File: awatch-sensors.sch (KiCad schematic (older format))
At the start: 35 parts, among them U501 BMM150, U502 APDS-9306-065, U503 BMI160, U504 BMP388

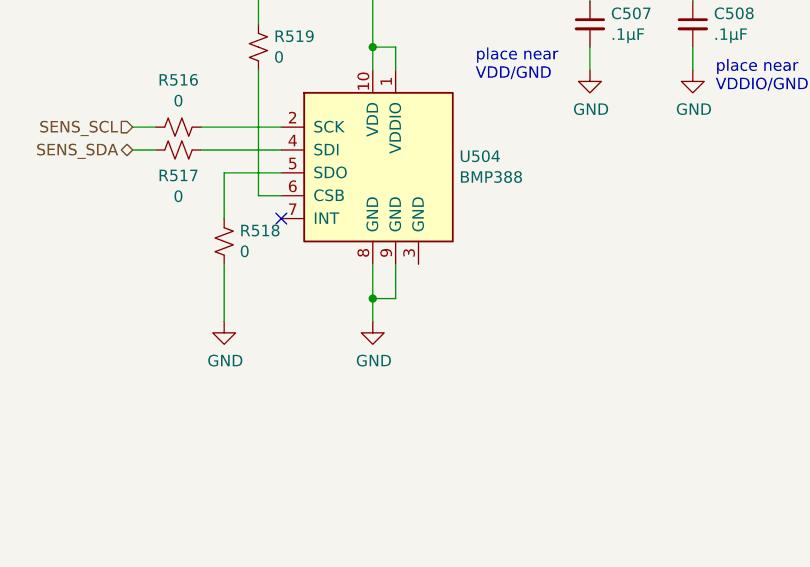
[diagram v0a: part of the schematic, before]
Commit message: Place and route pressure sensor.
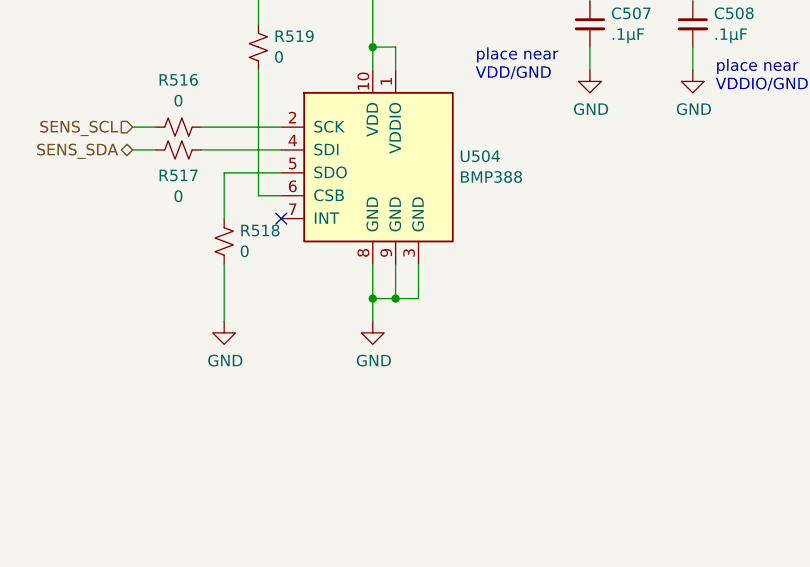
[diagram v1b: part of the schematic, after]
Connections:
- net GND: now also U504.3 (GND)
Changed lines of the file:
@@
 Wire Wire Line
 	10350 2450 10350 2500
+Wire Wire Line
+	9050 3800 9150 3800
+Wire Wire Line
+	9150 3800 9150 3650
+Connection ~ 9050 3800
 $EndSCHEMATC

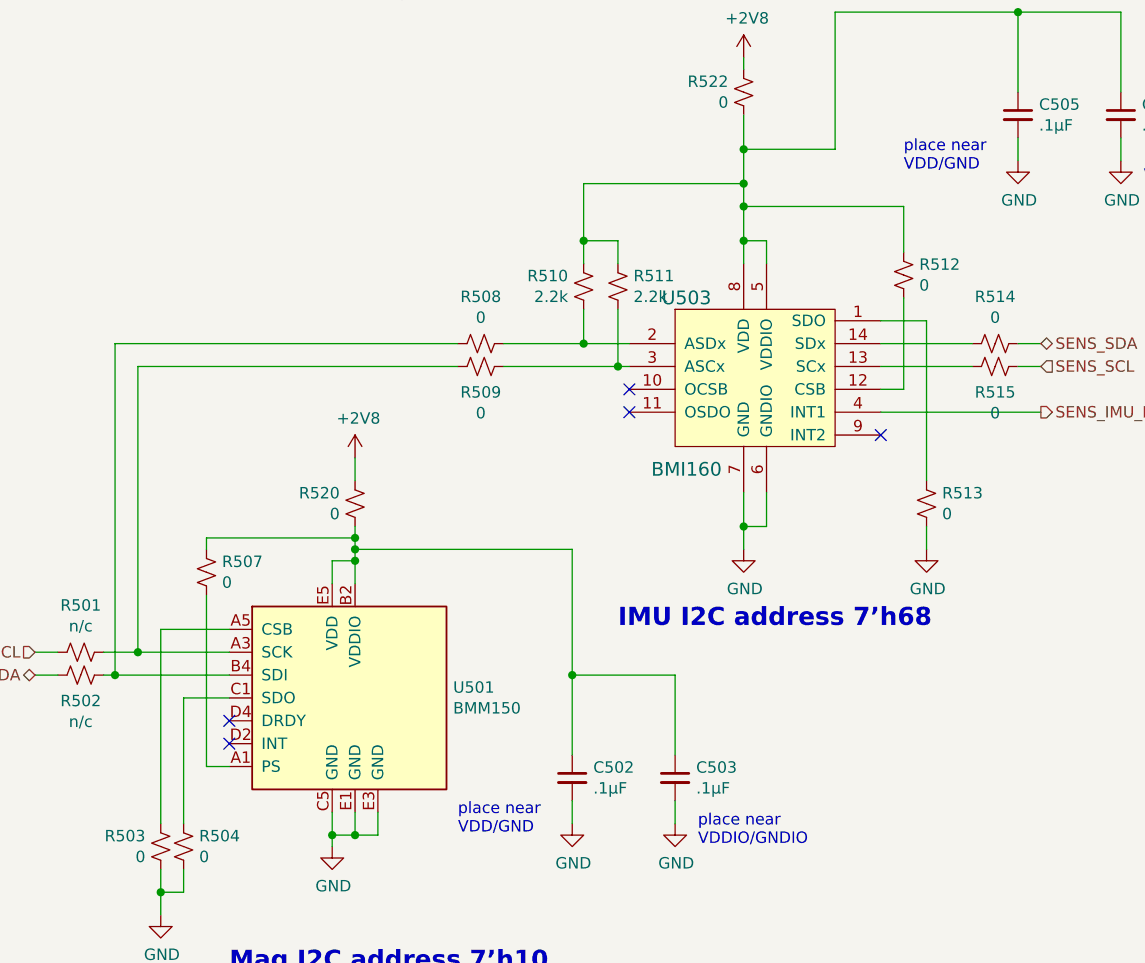
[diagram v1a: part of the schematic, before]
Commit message: IMU and magnetometer placed and routed
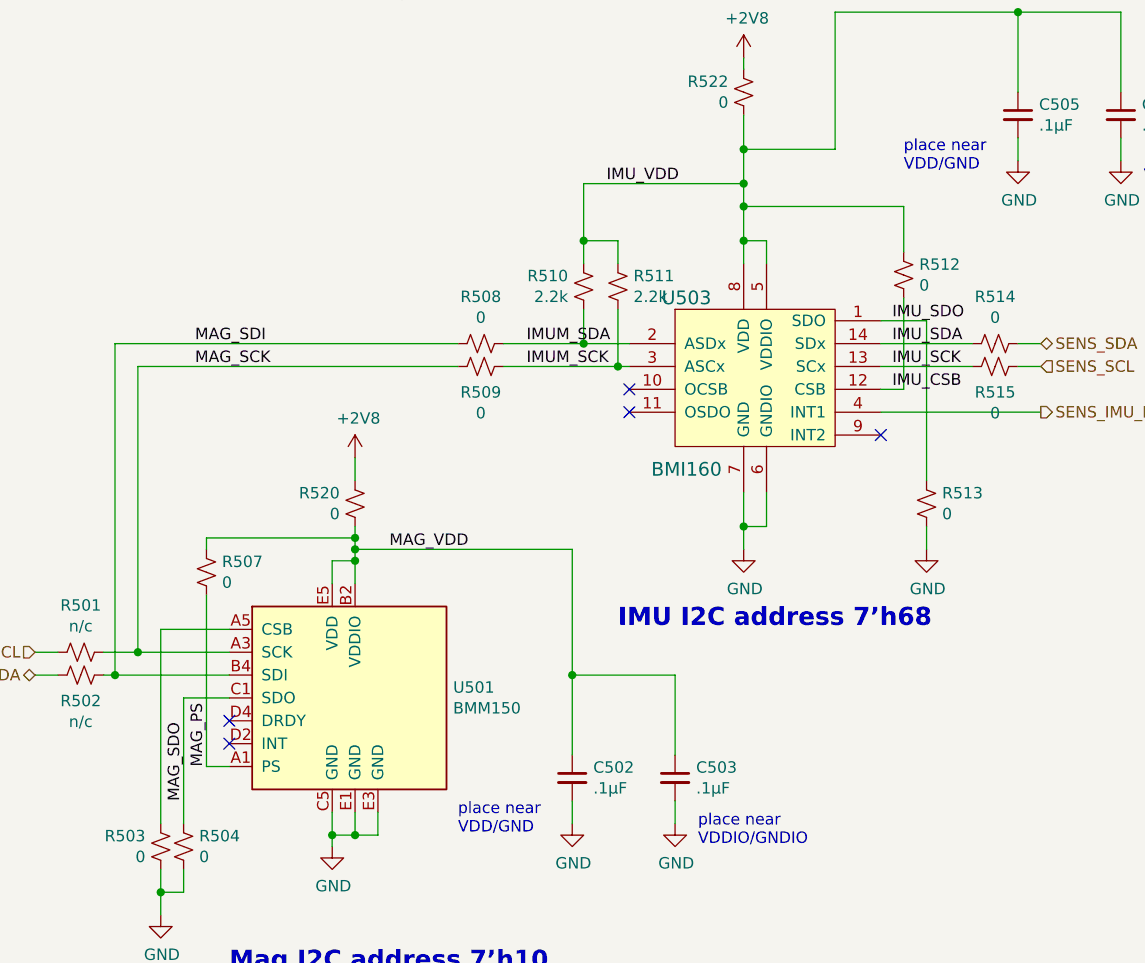
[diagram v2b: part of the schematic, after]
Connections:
- net IMU_SDO: now reaches R513.2, U503.1 (SDO)
- net IMU_CSB: now reaches R512.1, U503.12 (CSB)
- net IMU_SCK: now reaches R515.2, U503.13 (SCx)
- net IMU_SDA: now reaches R514.2, U503.14 (SDx)
- net IMUM_SDA: now reaches R508.1, R510.2, U503.2 (ASDx)
- net IMUM_SCK: now reaches R509.1, R511.2, U503.3 (ASCx)
- net IMU_VDD: now reaches C505.1, C506.1, R510.1, R511.1, R512.2, R522.1, U503.5 (VDDIO), U503.8 (VDD)
- net MAG_SDI: now reaches R502.1, R508.2, U501.B4 (SDI)
- net MAG_SCK: now reaches R501.1, R509.2, U501.A3 (SCK)
- net MAG_VDD: now reaches C502.1, C503.1, R507.2, R520.1, U501.B2 (VDDIO), U501.E5 (VDD)
- net MAG_PS: now reaches R507.1, U501.A1 (PS)
- net MAG_SDO: now reaches R504.2, U501.C1 (SDO)
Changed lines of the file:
@@
 	9150 3800 9150 3650
 Connection ~ 9050 3800
+Text Label 1900 4350 0    50   ~ 0
+MAG_SCK
+Text Label 1900 4250 0    50   ~ 0
+MAG_SDI
+Text Label 1850 6250 1    50   ~ 0
+MAG_SDO
+Text Label 1950 6100 1    50   ~ 0
+MAG_PS
+Text Label 2750 5150 0    50   ~ 0
+MAG_VDD
+Text Label 3350 4250 0    50   ~ 0
+IMUM_SDA
+Text Label 3350 4350 0    50   ~ 0
+IMUM_SCK
+Text Label 3700 3550 0    50   ~ 0
+IMU_VDD
+Text Label 4950 4250 0    50   ~ 0
+IMU_SDA
+Text Label 4950 4350 0    50   ~ 0
+IMU_SCK
+Text Label 4950 4450 0    50   ~ 0
+IMU_CSB
+Text Label 4950 4150 0    50   ~ 0
+IMU_SDO
 $EndSCHEMATC

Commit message: approx. final layout
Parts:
- C501, C504: value 1µF -> 1.0µF X7R; DigiKey PN (none) -> 1276-1946-1-ND
- C502, C503, C505, C506, C507, C508: value .1µF -> 0.1µF X7R; DigiKey PN (none) -> 1276-1061-1-ND
- U501: DigiKey PN (none) -> 828-1044-1-ND
- U502: DigiKey PN (none) -> 516-3578-1-ND
- U503: DigiKey PN (none) -> 828-1057-1-ND
- U504: DigiKey PN (none) -> 828-1079-1-ND
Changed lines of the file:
@@
 $Descr A4 11693 8268
 encoding utf-8
-Sheet 5 9
+Sheet 5 10
 Title "AWatch2"
 Date ""
@@
 F 2 "awatch2-footprints:DFN-6_2x2mm_P0.53mm" H 2200 1650 50  0001 C CNN
 F 3 "" H 2200 1650 50  0001 C CNN
+F 4 "516-3578-1-ND" H 0   0   50  0001 C CNN "DigiKey PN"
 	1    2200 1650
 	1    0    0    -1
@@
 P 3100 1950
 F 0 "C501" H 3192 1996 50  0000 L CNN
-F 1 "1µF" H 3192 1905 50  0000 L CNN
+F 1 "1.0µF X7R" H 3192 1905 50  0000 L CNN
 F 2 "Capacitor_SMD:C_0603_1608Metric" H 3100 1950 50  0001 C CNN
 F 3 "~" H 3100 1950 50  0001 C CNN
+F 4 "1276-1946-1-ND" H 0   0   50  0001 C CNN "DigiKey PN"
 	1    3100 1950
 	1    0    0    -1
@@
 F 2 "awatch2-footprints:BMI160" H 4050 4650 60  0001 C CNN
 F 3 "" H 4050 4650 60  0001 C CNN
+F 4 "828-1057-1-ND" H 0   0   50  0001 C CNN "DigiKey PN"
 	1    4350 4400
 	1    0    0    -1
@@
 P 3550 6150
 F 0 "C502" H 3642 6196 50  0000 L CNN
-F 1 ".1µF" H 3642 6105 50  0000 L CNN
+F 1 "0.1µF X7R" H 3642 6105 50  0000 L CNN
 F 2 "Capacitor_SMD:C_0603_1608Metric" H 3550 6150 50  0001 C CNN
 F 3 "~" H 3550 6150 50  0001 C CNN
+F 4 "1276-1061-1-ND" H 0   0   50  0001 C CNN "DigiKey PN"
 	1    3550 6150
 	1    0    0    -1
@@
 P 4000 6150
 F 0 "C503" H 4092 6196 50  0000 L CNN
-F 1 ".1µF" H 4092 6105 50  0000 L CNN
+F 1 "0.1µF X7R" H 4092 6105 50  0000 L CNN
 F 2 "Capacitor_SMD:C_0603_1608Metric" H 4000 6150 50  0001 C CNN
 F 3 "~" H 4000 6150 50  0001 C CNN
+F 4 "1276-1061-1-ND" H 0   0   50  0001 C CNN "DigiKey PN"
 	1    4000 6150
 	1    0    0    -1
@@
 F 2 "awatch2-footprints:WLCSP-12_1.56x1.56mm_Layout5x5_P0.283mm_Ball0.25mm_Pad0.2mm_NSMD" H 2050 5300 50  0001 C CNN
 F 3 "" H 2050 5300 50  0001 C CNN
+F 4 "828-1044-1-ND" H 0   0   50  0001 C CNN "DigiKey PN"
 	1    2050 5300
 	1    0    0    -1
@@
 P 5500 3250
 F 0 "C505" H 5592 3296 50  0000 L CNN
-F 1 ".1µF" H 5592 3205 50  0000 L CNN
+F 1 "0.1µF X7R" H 5592 3205 50  0000 L CNN
 F 2 "Capacitor_SMD:C_0603_1608Metric" H 5500 3250 50  0001 C CNN
 F 3 "~" H 5500 3250 50  0001 C CNN
+F 4 "1276-1061-1-ND" H 0   0   50  0001 C CNN "DigiKey PN"
 	1    5500 3250
 	1    0    0    -1
@@
 P 5950 3250
 F 0 "C506" H 6042 3296 50  0000 L CNN
-F 1 ".1µF" H 6042 3205 50  0000 L CNN
+F 1 "0.1µF X7R" H 6042 3205 50  0000 L CNN
 F 2 "Capacitor_SMD:C_0603_1608Metric" H 5950 3250 50  0001 C CNN
 F 3 "~" H 5950 3250 50  0001 C CNN
+F 4 "1276-1061-1-ND" H 0   0   50  0001 C CNN "DigiKey PN"
 	1    5950 3250
 	1    0    0    -1
@@
 F 2 "awatch2-footprints:BMP388" H 8550 2900 50  0001 C CNN
 F 3 "" H 8550 2900 50  0001 C CNN
+F 4 "828-1079-1-ND" H 0   0   50  0001 C CNN "DigiKey PN"
 	1    8550 2900
 	1    0    0    -1
@@
 P 9900 2600
 F 0 "C507" H 9992 2646 50  0000 L CNN
-F 1 ".1µF" H 9992 2555 50  0000 L CNN
+F 1 "0.1µF X7R" H 9992 2555 50  0000 L CNN
 F 2 "Capacitor_SMD:C_0603_1608Metric" H 9900 2600 50  0001 C CNN
 F 3 "~" H 9900 2600 50  0001 C CNN
+F 4 "1276-1061-1-ND" H 0   0   50  0001 C CNN "DigiKey PN"
 	1    9900 2600
 	1    0    0    -1
@@
 P 10350 2600
 F 0 "C508" H 10442 2646 50  0000 L CNN
-F 1 ".1µF" H 10442 2555 50  0000 L CNN
+F 1 "0.1µF X7R" H 10442 2555 50  0000 L CNN
 F 2 "Capacitor_SMD:C_0603_1608Metric" H 10350 2600 50  0001 C CNN
 F 3 "~" H 10350 2600 50  0001 C CNN
+F 4 "1276-1061-1-ND" H 0   0   50  0001 C CNN "DigiKey PN"
 	1    10350 2600
 	1    0    0    -1
@@
 P 4450 1650
 F 0 "C504" H 4542 1696 50  0000 L CNN
-F 1 "1µF" H 4542 1605 50  0000 L CNN
+F 1 "1.0µF X7R" H 4542 1605 50  0000 L CNN
 F 2 "Capacitor_SMD:C_0603_1608Metric" H 4450 1650 50  0001 C CNN
 F 3 "~" H 4450 1650 50  0001 C CNN
+F 4 "1276-1946-1-ND" H 0   0   50  0001 C CNN "DigiKey PN"
 	1    4450 1650
 	1    0    0    -1

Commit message: BOM fully populated
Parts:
- R503, R504, R505, R506, R507, R508, R509, R512, R513, R514, R515, R516, R517, R518, R519, R520, R521, R522, R523: DigiKey PN (none) -> MCT0603-0.0-ZZCT-ND
- R510, R511: DigiKey PN (none) -> MCT0603-2.20K-CFCT-ND
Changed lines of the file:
@@
 F 2 "Resistor_SMD:R_0603_1608Metric" H 1900 1850 50  0001 C CNN
 F 3 "~" H 1900 1850 50  0001 C CNN
+F 4 "MCT0603-0.0-ZZCT-ND" H 0   0   50  0001 C CNN "DigiKey PN"
 	1    1900 1850
 	0    1    1    0
@@
 F 2 "Resistor_SMD:R_0603_1608Metric" H 1900 1950 50  0001 C CNN
 F 3 "~" H 1900 1950 50  0001 C CNN
+F 4 "MCT0603-0.0-ZZCT-ND" H 0   0   50  0001 C CNN "DigiKey PN"
 	1    1900 1950
 	0    1    1    0
@@
 F 2 "Resistor_SMD:R_0603_1608Metric" H 5000 3950 50  0001 C CNN
 F 3 "~" H 5000 3950 50  0001 C CNN
+F 4 "MCT0603-0.0-ZZCT-ND" H 0   0   50  0001 C CNN "DigiKey PN"
 	1    5000 3950
 	-1   0    0    1
@@
 F 2 "Resistor_SMD:R_0603_1608Metric" H 5100 4950 50  0001 C CNN
 F 3 "~" H 5100 4950 50  0001 C CNN
+F 4 "MCT0603-0.0-ZZCT-ND" H 0   0   50  0001 C CNN "DigiKey PN"
 	1    5100 4950
 	-1   0    0    1
@@
 F 2 "Resistor_SMD:R_0603_1608Metric" H 5400 4350 50  0001 C CNN
 F 3 "~" H 5400 4350 50  0001 C CNN
+F 4 "MCT0603-0.0-ZZCT-ND" H 0   0   50  0001 C CNN "DigiKey PN"
 	1    5400 4350
 	0    1    1    0
@@
 F 2 "Resistor_SMD:R_0603_1608Metric" H 5400 4250 50  0001 C CNN
 F 3 "~" H 5400 4250 50  0001 C CNN
+F 4 "MCT0603-0.0-ZZCT-ND" H 0   0   50  0001 C CNN "DigiKey PN"
 	1    5400 4250
 	0    1    1    0
@@
 F 2 "Resistor_SMD:R_0603_1608Metric" H 3150 4250 50  0001 C CNN
 F 3 "~" H 3150 4250 50  0001 C CNN
+F 4 "MCT0603-0.0-ZZCT-ND" H 0   0   50  0001 C CNN "DigiKey PN"
 	1    3150 4250
 	0    1    1    0
@@
 F 2 "Resistor_SMD:R_0603_1608Metric" H 3150 4350 50  0001 C CNN
 F 3 "~" H 3150 4350 50  0001 C CNN
+F 4 "MCT0603-0.0-ZZCT-ND" H 0   0   50  0001 C CNN "DigiKey PN"
 	1    3150 4350
 	0    1    1    0
@@
 F 2 "Resistor_SMD:R_0603_1608Metric" H 3600 4000 50  0001 C CNN
 F 3 "~" H 3600 4000 50  0001 C CNN
+F 4 "MCT0603-2.20K-CFCT-ND" H 0   0   50  0001 C CNN "DigiKey PN"
 	1    3600 4000
 	1    0    0    -1
@@
 F 2 "Resistor_SMD:R_0603_1608Metric" H 3750 4000 50  0001 C CNN
 F 3 "~" H 3750 4000 50  0001 C CNN
+F 4 "MCT0603-2.20K-CFCT-ND" H 0   0   50  0001 C CNN "DigiKey PN"
 	1    3750 4000
 	1    0    0    -1
@@
 F 2 "Resistor_SMD:R_0603_1608Metric" H 1750 6450 50  0001 C CNN
 F 3 "~" H 1750 6450 50  0001 C CNN
+F 4 "MCT0603-0.0-ZZCT-ND" H 0   0   50  0001 C CNN "DigiKey PN"
 	1    1750 6450
 	-1   0    0    1
@@
 F 2 "Resistor_SMD:R_0603_1608Metric" H 1850 6450 50  0001 C CNN
 F 3 "~" H 1850 6450 50  0001 C CNN
+F 4 "MCT0603-0.0-ZZCT-ND" H 0   0   50  0001 C CNN "DigiKey PN"
 	1    1850 6450
 	-1   0    0    1
@@
 F 2 "Resistor_SMD:R_0603_1608Metric" H 1950 5250 50  0001 C CNN
 F 3 "~" H 1950 5250 50  0001 C CNN
+F 4 "MCT0603-0.0-ZZCT-ND" H 0   0   50  0001 C CNN "DigiKey PN"
 	1    1950 5250
 	-1   0    0    1
@@
 F 2 "Resistor_SMD:R_0603_1608Metric" H 8450 2700 50  0001 C CNN
 F 3 "~" H 8450 2700 50  0001 C CNN
+F 4 "MCT0603-0.0-ZZCT-ND" H 0   0   50  0001 C CNN "DigiKey PN"
 	1    8450 2700
 	-1   0    0    1
@@
 F 2 "Resistor_SMD:R_0603_1608Metric" H 8100 3050 50  0001 C CNN
 F 3 "~" H 8100 3050 50  0001 C CNN
+F 4 "MCT0603-0.0-ZZCT-ND" H 0   0   50  0001 C CNN "DigiKey PN"
 	1    8100 3050
 	0    1    1    0
@@
 F 2 "Resistor_SMD:R_0603_1608Metric" H 8100 3150 50  0001 C CNN
 F 3 "~" H 8100 3150 50  0001 C CNN
+F 4 "MCT0603-0.0-ZZCT-ND" H 0   0   50  0001 C CNN "DigiKey PN"
 	1    8100 3150
 	0    1    1    0
@@
 F 2 "Resistor_SMD:R_0603_1608Metric" H 8300 3550 50  0001 C CNN
 F 3 "~" H 8300 3550 50  0001 C CNN
+F 4 "MCT0603-0.0-ZZCT-ND" H 0   0   50  0001 C CNN "DigiKey PN"
 	1    8300 3550
 	-1   0    0    1
@@
 F 2 "Resistor_SMD:R_0603_1608Metric" H 2850 1250 50  0001 C CNN
 F 3 "~" H 2850 1250 50  0001 C CNN
+F 4 "MCT0603-0.0-ZZCT-ND" H 0   0   50  0001 C CNN "DigiKey PN"
 	1    2850 1250
 	-1   0    0    1
@@
 F 2 "Resistor_SMD:R_0603_1608Metric" H 4300 3150 50  0001 C CNN
 F 3 "~" H 4300 3150 50  0001 C CNN
+F 4 "MCT0603-0.0-ZZCT-ND" H 0   0   50  0001 C CNN "DigiKey PN"
 	1    4300 3150
 	-1   0    0    1
@@
 F 2 "Resistor_SMD:R_0603_1608Metric" H 2600 4950 50  0001 C CNN
 F 3 "~" H 2600 4950 50  0001 C CNN
+F 4 "MCT0603-0.0-ZZCT-ND" H 0   0   50  0001 C CNN "DigiKey PN"
 	1    2600 4950
 	-1   0    0    1
@@
 F 2 "Resistor_SMD:R_0603_1608Metric" H 8950 2300 50  0001 C CNN
 F 3 "~" H 8950 2300 50  0001 C CNN
+F 4 "MCT0603-0.0-ZZCT-ND" H 0   0   50  0001 C CNN "DigiKey PN"
 	1    8950 2300
 	-1   0    0    1
